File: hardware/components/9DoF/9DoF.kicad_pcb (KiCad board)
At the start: 2 copper layers, 12 parts, among them U101 BMI088, U102 QMC5883L

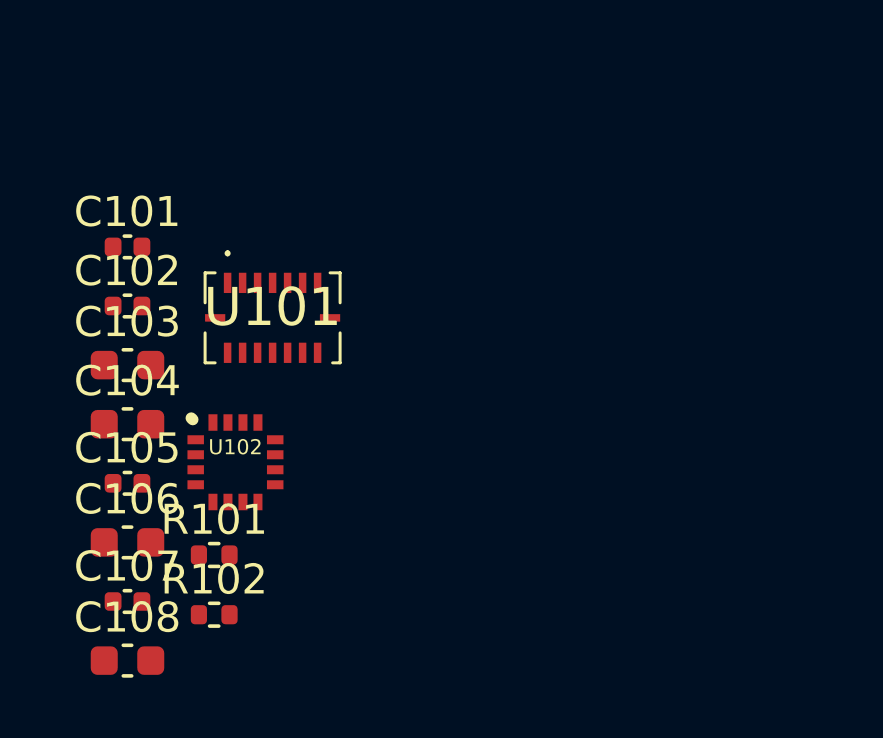
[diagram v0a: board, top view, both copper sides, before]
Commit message: 9DoFの配線をしました
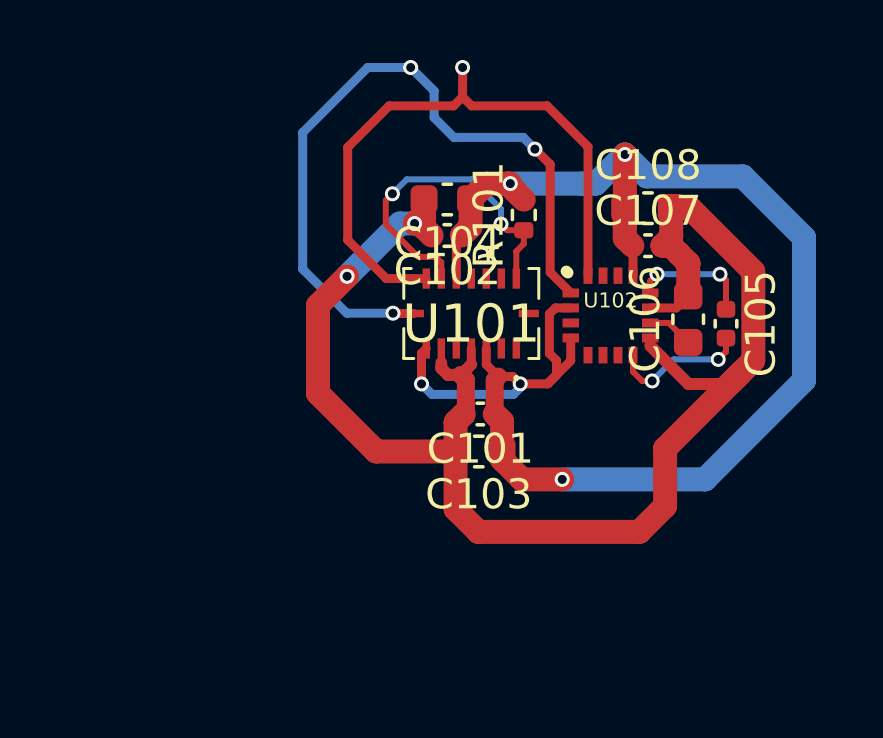
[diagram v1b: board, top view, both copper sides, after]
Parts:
- removed R102: 4.7K, Resistor_SMD:R_0402_1005Metric
- moved C108 23.0 mm to (161.9, 83.5)
- moved C107 21.0 mm to (161.9, 84.7)
- moved C105 20.6 mm to (164.6, 87.3), turned to -90 degrees
- moved C106 20.1 mm to (163.3, 87.2), turned to 90 degrees
- moved R101 15.3 mm to (157.8, 83.7), turned to 90 degrees
- moved U102 13.4 mm to (160.7, 87.0)
- moved C104 13.0 mm to (155.3, 83.2), turned to 180 degrees
- moved C101 13.0 mm to (156.4, 90.3), turned to 180 degrees
- moved C103 12.1 mm to (156.3, 91.6), turned to 180 degrees
- moved C102 10.9 mm to (155.3, 84.4), turned to 180 degrees
- moved U101 6.62 mm to (156.1, 87.0), turned to 180 degrees
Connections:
- net 3V3 renamed VDD
- net SCL renamed /I2C_SCL
- net SDA renamed /I2C_SDA
- R101 pad 1: AD0 -> Net-(U101-SDO1)
- U101 pad 10: AD1 -> Net-(U101-SDO1)
- U101 pad 15: AD0 -> Net-(U101-SDO1)
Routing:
- net VDD: track 0.00 -> 53.0 mm, vias 0 -> 5
- net GND: track 0.00 -> 50.3 mm, vias 0 -> 2
- net /I2C_SCL: track 0.00 -> 24.4 mm, vias 0 -> 3
- net /I2C_SDA: track 0.00 -> 20.9 mm, vias 0 -> 1
- net Net-(U101-SDO1): track 0.00 -> 11.4 mm, vias 0 -> 2
- net Net-(U102-STEP): track 0.00 -> 4.63 mm, vias 0 -> 2
- net Net-(U102-SETC): track 0.00 -> 4.07 mm, vias 0 -> 2
- net Net-(U102-C1): track 0.00 -> 1.53 mm

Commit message: ちょっと修正しました
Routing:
- net /I2C_SDA: track 20.9 -> 19.7 mm, vias 1 -> 0
- net /I2C_SCL: vias 3 -> 2
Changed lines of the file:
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@@
 		(tags "resistor")
 		(property "Reference" "R101"
-			(at 0 -1.17 270)
+			(at 2.815 0 -90)
 			(layer "F.SilkS")
 			(effects
@@
 		)
 		(property "Value" "4.7K"
-			(at 0 1.17 270)
+			(at 0 1.17 -90)
 			(layer "F.Fab")
 			(effects
@@
 		)
 		(fp_text user "${REFERENCE}"
-			(at 0 0 270)
+			(at 0 0 -90)
 			(layer "F.Fab")
 			(effects
@@
 		(tags "capacitor")
 		(property "Reference" "C107"
-			(at 0 -1.16 360)
+			(at 3.45 -0.04 0)
 			(layer "F.SilkS")
 			(effects
@@
 		)
 		(property "Value" "100nF"
-			(at 0 1.16 360)
+			(at 0 1.16 0)
 			(layer "F.Fab")
 			(effects
@@
 		)
 		(fp_text user "${REFERENCE}"
-			(at 0 0 360)
+			(at 0 0 0)
 			(layer "F.Fab")
 			(effects
@@
 		(tags "capacitor")
 		(property "Reference" "C106"
-			(at 0 -1.43 270)
+			(at -3.35 0.19 -90)
 			(layer "F.SilkS")
 			(effects
@@
 		)
 		(property "Value" "4.7μF"
-			(at 0 1.43 270)
+			(at 0 1.43 -90)
 			(layer "F.Fab")
 			(effects
@@
 		)
 		(fp_text user "${REFERENCE}"
-			(at 0 0 270)
+			(at 0 0 -90)
 			(layer "F.Fab")
 			(effects
@@
 		(tags "capacitor")
 		(property "Reference" "C104"
-			(at 0 -1.43 180)
+			(at 3.5 0.05 180)
 			(layer "F.SilkS")
 			(effects
@@
 		(tags "Integrated Circuit")
 		(property "Reference" "U101"
-			(at 0 -0.349 180)
+			(at 4.68 -1.79 180)
 			(layer "F.SilkS")
 			(effects
@@
 		(tags "capacitor")
 		(property "Reference" "C102"
-			(at 0 -1.16 180)
+			(at 3.47 -0.07 180)
 			(layer "F.SilkS")
 			(effects
@@
 		(tags "capacitor")
 		(property "Reference" "C108"
-			(at 0 -1.43 360)
+			(at 3.58 -0.23 0)
 			(layer "F.SilkS")
 			(effects
@@
 		)
 		(property "Value" "10μF"
-			(at 0 1.43 360)
+			(at 0 1.43 0)
 			(layer "F.Fab")
 			(effects
@@
 		)
 		(fp_text user "${REFERENCE}"
-			(at 0 0 360)
+			(at 0 0 0)
 			(layer "F.Fab")
 			(effects
@@
 		(tags "capacitor")
 		(property "Reference" "C101"
-			(at 0 -1.16 180)
+			(at 3.45 -0.24 180)
 			(layer "F.SilkS")
 			(effects
@@
 		(tags "compass sensor, magnetometer")
 		(property "Reference" "U102"
-			(at 0 -0.5 360)
+			(at -0.32 3.485 0)
 			(layer "F.SilkS")
 			(effects
 				(font
-					(size 0.5 0.5)
-					(thickness 0.125)
+					(size 1.27 1.27)
+					(thickness 0.254)
+					(bold yes)
 				)
 			)
 		)
 		(property "Value" "QMC5883L"
-			(at 0 0.5 360)
+			(at 0 0.5 0)
 			(layer "F.SilkS")
 			(hide yes)
@@
 		(tags "capacitor")
 		(property "Reference" "C103"
-			(at 0 -1.43 180)
+			(at 3.4 -0.53 180)
 			(layer "F.SilkS")
 			(effects
@@
 		(start 156.06 88.6575)
 		(end 155.71 89.0075)
-		(width 0.4)
+		(width 0.3)
 		(layer "F.Cu")
 		(net 1)
@@
 	(via
 		(at 154.17 83.96)
-		(size 0.5)
-		(drill 0.3)
+		(size 1)
+		(drill 0.8)
 		(layers "F.Cu" "B.Cu")
 		(net 1)
@@
 	(via
 		(at 151.92 85.72)
-		(size 0.5)
-		(drill 0.3)
+		(size 1)
+		(drill 0.8)
 		(layers "F.Cu" "B.Cu")
 		(net 1)
@@
 	(via
 		(at 159.09 92.49)
-		(size 0.5)
-		(drill 0.3)
+		(size 1)
+		(drill 0.8)
 		(layers "F.Cu" "B.Cu")
 		(net 5)
@@
 	(via
 		(at 157.36 82.63)
-		(size 0.5)
-		(drill 0.3)
+		(size 1)
+		(drill 0.8)
 		(layers "F.Cu" "B.Cu")
 		(net 5)
@@
 	(via
 		(at 161.18 81.66)
-		(size 0.5)
-		(drill 0.3)
+		(size 1)
+		(drill 0.8)
 		(layers "F.Cu" "B.Cu")
 		(net 5)
@@
 	)
 	(segment
-		(start 153.21 83.98995)
-		(end 154.29505 85.075)
+		(start 153.28 82.79)
+		(end 153.02 83.05)
 		(width 0.2)
 		(layer "F.Cu")
@@
 	)
 	(segment
-		(start 157.56 84.8875)
-		(end 157.81 84.6375)
+		(start 154.115 85.075)
+		(end 154.8775 85.075)
 		(width 0.2)
 		(layer "F.Cu")
@@
 	)
 	(segment
-		(start 157.81 84.185)
+		(start 157.56 84.8875)
 		(end 157.81 84.6375)
 		(width 0.2)
@@
 	)
 	(segment
-		(start 157.81 84.185)
-		(end 157.2575 84.185)
+		(start 153.02 83.98)
+		(end 154.115 85.075)
 		(width 0.2)
 		(layer "F.Cu")
@@
 	)
 	(segment
-		(start 157.05 83.9775)
-		(end 157.1025 83.9775)
+		(start 155.06 85.2575)
+		(end 155.06 85.795)
 		(width 0.2)
 		(layer "F.Cu")
@@
 	)
 	(segment
-		(start 154.29505 85.075)
-		(end 154.8775 85.075)
+		(start 157.81 84.185)
+		(end 157.81 84.6375)
 		(width 0.2)
 		(layer "F.Cu")
@@
 	)
 	(segment
-		(start 157.2575 84.185)
-		(end 157.05 83.9775)
+		(start 157.81 84.185)
+		(end 157.2575 84.185)
 		(width 0.2)
 		(layer "F.Cu")
@@
 	)
 	(segment
-		(start 157.56 85.795)
-		(end 157.56 84.8875)
+		(start 157.05 83.9775)
+		(end 157.1025 83.9775)
 		(width 0.2)
 		(layer "F.Cu")
@@
 	)
 	(segment
-		(start 154.8775 85.075)
-		(end 155.06 85.2575)
+		(start 153.02 83.05)
+		(end 153.02 83.98)
 		(width 0.2)
 		(layer "F.Cu")
@@
 	)
 	(segment
-		(start 153.43 82.97)
-		(end 153.21 83.19)
+		(start 157.2575 84.185)
+		(end 157.05 83.9775)
 		(width 0.2)
 		(layer "F.Cu")
@@
 	)
 	(segment
-		(start 153.21 83.19)
-		(end 153.21 83.98995)
+		(start 157.56 85.795)
+		(end 157.56 84.8875)
 		(width 0.2)
 		(layer "F.Cu")
@@
 	)
 	(segment
-		(start 155.06 85.2575)
-		(end 155.06 85.795)
+		(start 154.8775 85.075)
+		(end 155.06 85.2575)
 		(width 0.2)
 		(layer "F.Cu")
@@
 	)
 	(via
-		(at 153.43 82.97)
+		(at 153.28 82.79)
 		(size 0.5)
 		(drill 0.3)
@@
 	)
 	(segment
-		(start 153.91 82.49)
-		(end 156.06 82.49)
+		(start 156.06 82.49)
+		(end 157.05 83.48)
 		(width 0.2)
 		(layer "B.Cu")
@@
 	)
 	(segment
-		(start 156.06 82.49)
-		(end 157.05 83.48)
+		(start 153.58 82.49)
+		(end 156.06 82.49)
 		(width 0.2)
 		(layer "B.Cu")
@@
 	)
 	(segment
-		(start 153.43 82.97)
-		(end 153.91 82.49)
+		(start 153.28 82.79)
+		(end 153.58 82.49)
 		(width 0.2)
 		(layer "B.Cu")
@@
 		(net 14)
 	)
-	(via
-		(at 154.04 78.76)
-		(size 0.5)
-		(drill 0.3)
-		(layers "F.Cu" "B.Cu")
-		(net 14)
-	)
 	(segment
 		(start 151.91 86.95)
@@
 	)
 	(segment
-		(start 153.225 85.795)
-		(end 151.94 84.51)
-		(width 0.3)
-		(layer "F.Cu")
-		(net 21)
-	)
-	(segment
-		(start 151.94 84.51)
-		(end 151.94 81.42)
-		(width 0.3)
-		(layer "F.Cu")
-		(net 21)
-	)
-	(segment
-		(start 156.07 80.04)
+		(start 159.95 81.4)
 		(end 158.59 80.04)
 		(width 0.3)
@@
 	)
 	(segment
-		(start 153.32 80.04)
-		(end 155.47 80.04)
-		(width 0.3)
-		(layer "F.Cu")
-		(net 21)
-	)
-	(segment
-		(start 155.77 79.74)
-		(end 155.77 78.76)
-		(width 0.3)
-		(layer "F.Cu")
-		(net 21)
-	)
-	(segment
-		(start 154.56 85.795)
-		(end 153.225 85.795)
+		(start 159.95 85.7)
+		(end 159.95 81.4)
 		(width 0.3)
 		(layer "F.Cu")
@@
 	)
 	(segment
-		(start 151.94 81.42)
-		(end 153.32 80.04)
+		(start 153.32 80.04)
+		(end 151.94 81.42)
 		(width 0.3)
 		(layer "F.Cu")
@@
 	)
 	(segment
-		(start 156.07 80.04)
-		(end 155.77 79.74)
+		(start 153.225 85.795)
+		(end 154.56 85.795)
 		(width 0.3)
 		(layer "F.Cu")
@@
 	(segment
 		(start 158.59 80.04)
-		(end 159.95 81.4)
+		(end 153.32 80.04)
 		(width 0.3)
 		(layer "F.Cu")
@@
 	)
 	(segment
-		(start 159.95 81.4)
-		(end 159.95 85.7)
+		(start 151.94 81.42)
+		(end 151.94 84.51)
 		(width 0.3)
 		(layer "F.Cu")
@@
 	)
 	(segment
-		(start 155.47 80.04)
-		(end 155.77 79.74)
+		(start 151.94 84.51)
+		(end 153.225 85.795)
 		(width 0.3)
 		(layer "F.Cu")
 		(net 21)
 	)
-	(via
-		(at 155.77 78.76)
-		(size 0.5)
-		(drill 0.3)
-		(layers "F.Cu" "B.Cu")
-		(net 21)
-	)
